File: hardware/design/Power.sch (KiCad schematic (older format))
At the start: 11 parts

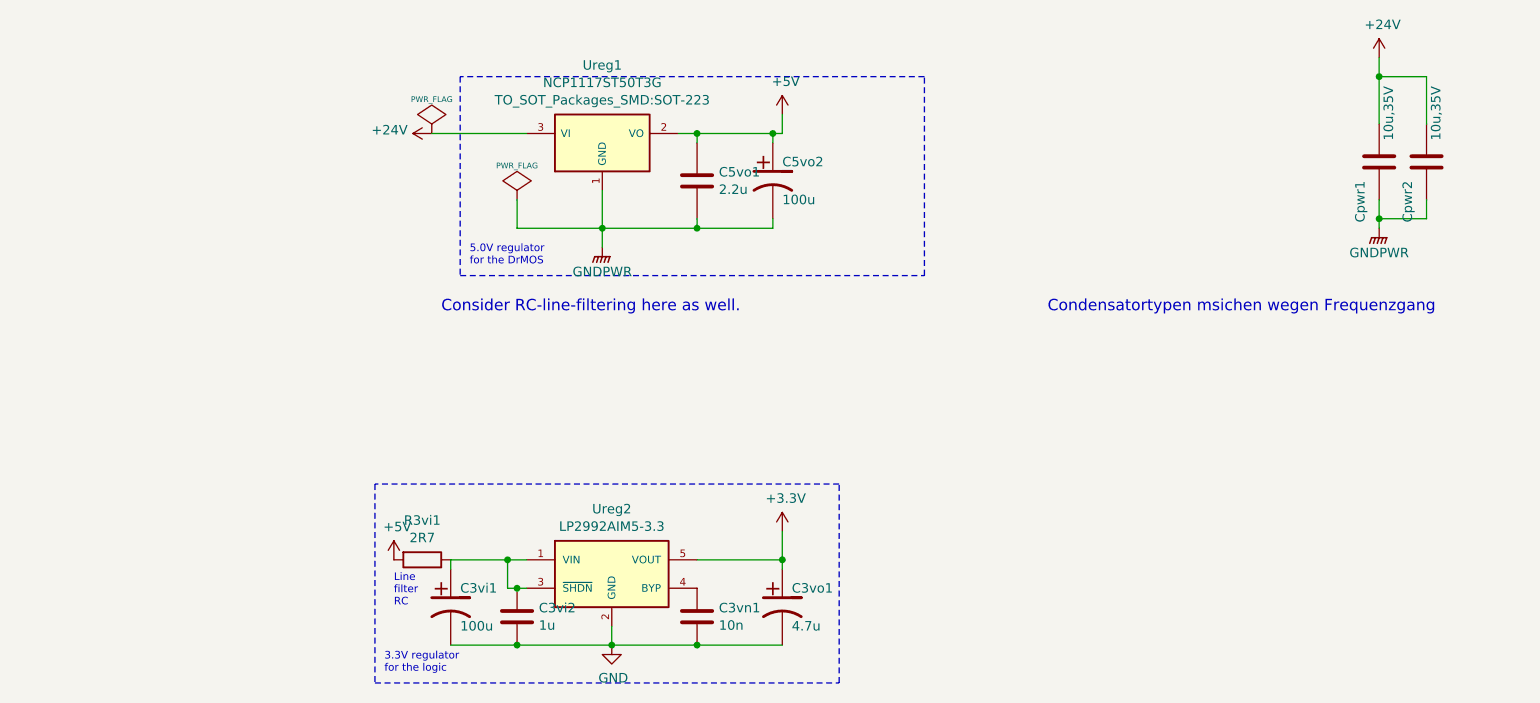
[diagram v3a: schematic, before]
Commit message: Created new component and footprint for regulator LTM8020.
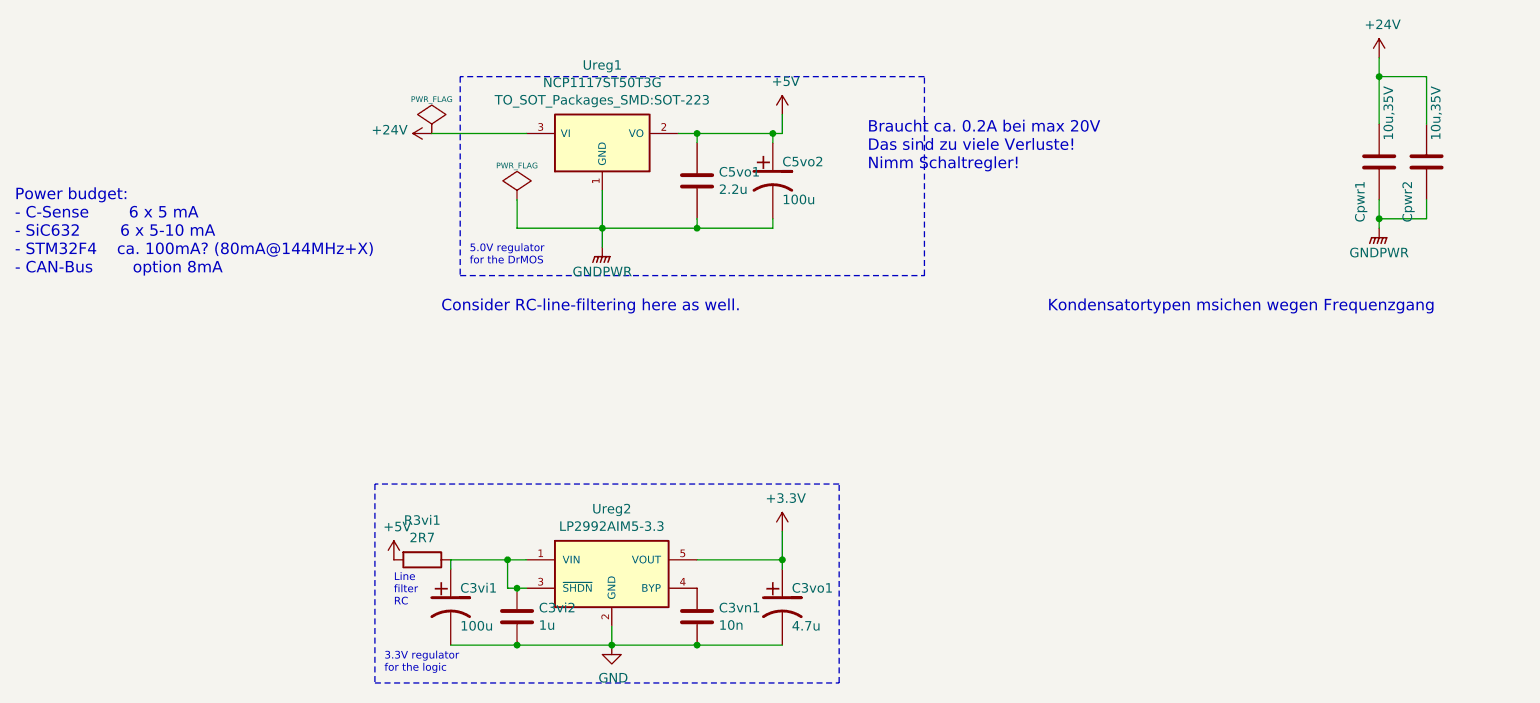
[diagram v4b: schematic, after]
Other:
- note added: "Braucht ca. 0.2A bei max 20V\nDas sind zu viele Verluste!\nNimm Schaltregler!"
- note added: "Kondensatortypen msichen wegen Frequenzgang"
- note added: "Power budget:\n- C-Sense 6 x 5 mA\n- SiC632 6 x 5-10 mA\n- STM32F4 ca. 100mA? (80mA@144MHz+X)\n- CAN-Bus option 8mA"
- note removed: "Condensatortypen msichen wegen Frequenzgang"
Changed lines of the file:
@@
 $Descr A4 11693 8268
 encoding utf-8
-Sheet 5 11
+Sheet 4 11
 Title "DrChibi"
 Date "25 Aug 2014"
@@
 00 FD 87 A8 17 00 00 00 00 F4 1F A2 5E 00 00 00 00 D0 7F 88 7A 01 00 00 00 40 FF 21 EA 05 00 00
 00 00 FD 87 A8 17 00 00 00 00 F4 1F A2 5E 00 00 00 00 D0 7F 88 7A 01 00 00 00 40 FF 21 EA 05 00
-00 00 00 FD F7 3F 90 37 91 24 49 74 FD E2 00 00 00 00 49 45 4E 44 AE 42 60 82 0F
+00 00 00 FD F7 3F 90 37 91 24 49 74 FD E2 00 00 00 00 49 45 4E 44 AE 42 60 82 00
 EndData
 $EndBitmap
@@
 AB D8 39 0B 59 91 9E DF A8 2A 5B EE 54 3A FD 71 ED 71 2F 29 C3 82 EC 80 87 06 6E C3 98 10 30 3B
 62 9A BB 2D 03 B8 C4 64 FC B5 26 AC 13 9B D1 39 40 41 C1 D6 78 4C 84 BF 94 F0 6F E1 BF 96 F0 0F
-FF 77 E2 FF 1F 0F 43 55 32 21 1C 08 16 00 00 00 00 49 45 4E 44 AE 42 60 82 EE
+FF 77 E2 FF 1F 0F 43 55 32 21 1C 08 16 00 00 00 00 49 45 4E 44 AE 42 60 82 A8
 EndData
 $EndBitmap
@@
 Connection ~ 5850 3850
 Text Notes 8650 2100 0    60   ~ 0
-Condensatortypen msichen wegen Frequenzgang
+Kondensatortypen msichen wegen Frequenzgang
 Text Notes 5200 3650 0    40   ~ 0
 Line\nfilter\nRC
 Text Notes 5450 2100 0    60   ~ 0
 Consider RC-line-filtering here as well.
+Text Notes 7700 1350 0    60   ~ 0
+Braucht ca. 0.2A bei max 20V\nDas sind zu viele Verluste!\nNimm Schaltregler!
+Text Notes 3200 1900 0    60   ~ 0
+Power budget:\n- C-Sense		6 x 5 mA\n- SiC632		6 x 5-10 mA\n- STM32F4	ca. 100mA? (80mA@144MHz+X)\n- CAN-Bus		option 8mA
 $EndSCHEMATC

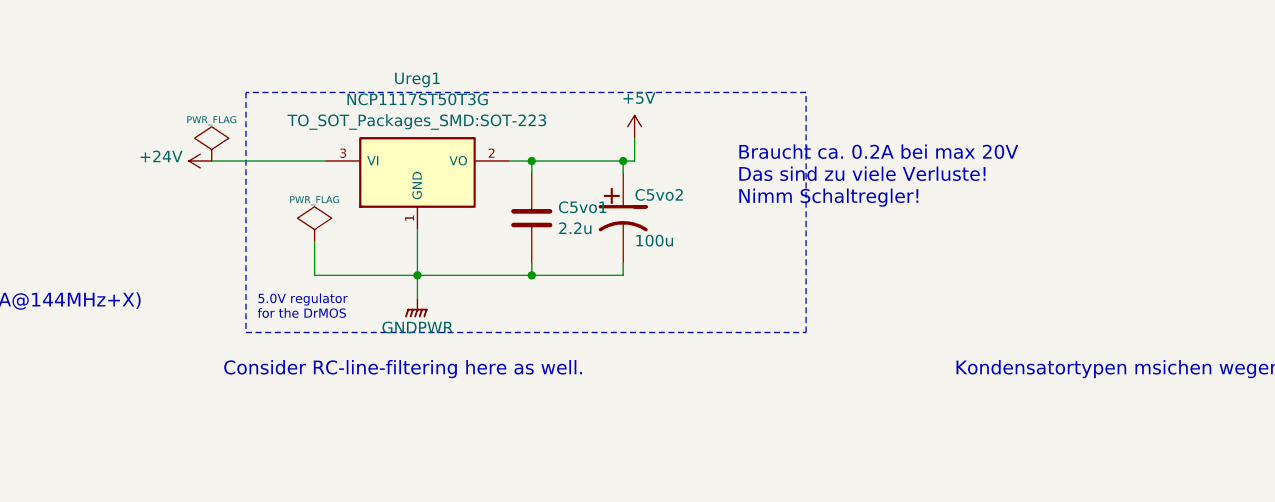
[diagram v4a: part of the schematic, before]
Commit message: Added the 5V regulator LTM8020 to the schematic.
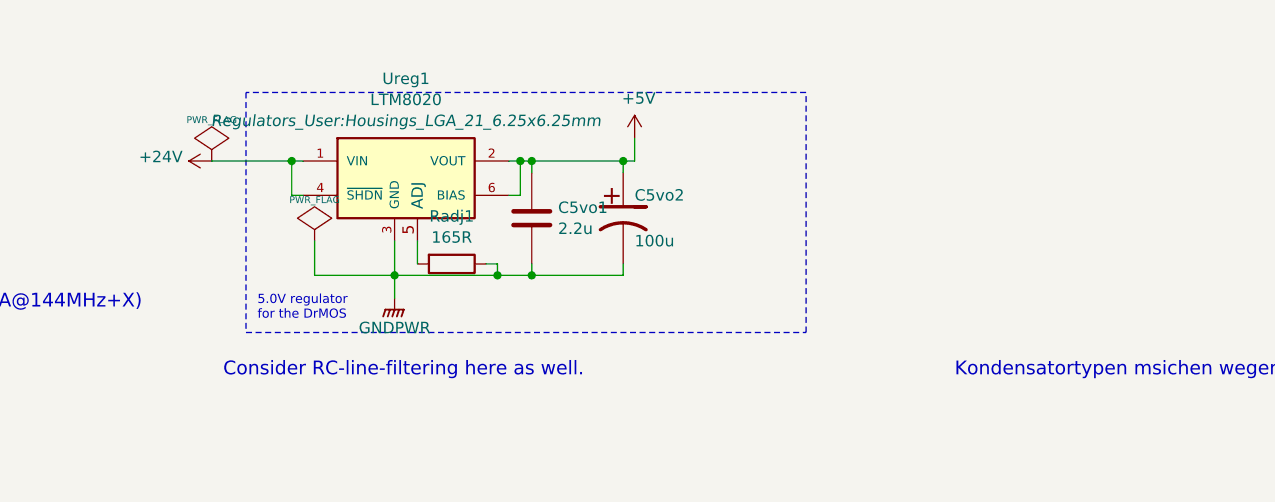
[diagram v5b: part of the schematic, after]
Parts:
- removed Ureg1: NCP1117ST50T3G, TO_SOT_Packages_SMD:SOT-223, symbol NCP1117ST50T3G
- added Radj1: 165R, Resistors_SMD:R_0402, symbol R
- added Ureg1: LTM8020, Regulators_User:Housings_LGA_21_6.25x6.25mm, symbol LTM8020
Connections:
- net +24V: now also Ureg1.1 (VIN), Ureg1.4 (~SHDN~)
- net +5V: now also Ureg1.2 (VOUT), Ureg1.6 (BIAS)
- net GNDPWR: now also Radj1.1, Ureg1.3 (GND)
- new net: Radj1.2, Ureg1.5 (ADJ)
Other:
- note removed: "Braucht ca. 0.2A bei max 20V\nDas sind zu viele Verluste!\nNimm Schaltregler!"
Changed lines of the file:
@@
 LIBS:pkl_drmos
 LIBS:pkl_misc
+LIBS:pkl_regulator
 LIBS:DrChibi-cache
 EELAYER 25 0
@@
 	7200 1650 7200 1600
 Wire Wire Line
-	6300 1450 6300 1750
-Wire Wire Line
 	6800 1650 6800 1600
-Connection ~ 6300 1650
+Connection ~ 6200 1650
 Wire Wire Line
 	7250 1150 7250 1050
@@
 AB D8 39 0B 59 91 9E DF A8 2A 5B EE 54 3A FD 71 ED 71 2F 29 C3 82 EC 80 87 06 6E C3 98 10 30 3B
 62 9A BB 2D 03 B8 C4 64 FC B5 26 AC 13 9B D1 39 40 41 C1 D6 78 4C 84 BF 94 F0 6F E1 BF 96 F0 0F
-FF 77 E2 FF 1F 0F 43 55 32 21 1C 08 16 00 00 00 00 49 45 4E 44 AE 42 60 82 A8
+FF 77 E2 FF 1F 0F 43 55 32 21 1C 08 16 00 00 00 00 49 45 4E 44 AE 42 60 82 14
 EndData
 $EndBitmap
-Wire Wire Line
-	5900 1150 5400 1150
 $Comp
 L GNDPWR #PWR030
 U 1 1 55E7501A
-P 6300 1750
-F 0 "#PWR030" H 6300 1550 50  0001 C CNN
-F 1 "GNDPWR" H 6300 1620 50  0000 C CNN
-F 2 "" H 6300 1700 60  0000 C CNN
-F 3 "" H 6300 1700 60  0000 C CNN
-	1    6300 1750
+P 6200 1750
+F 0 "#PWR030" H 6200 1550 50  0001 C CNN
+F 1 "GNDPWR" H 6200 1620 50  0000 C CNN
+F 2 "" H 6200 1700 60  0000 C CNN
+F 3 "" H 6200 1700 60  0000 C CNN
+	1    6200 1750
 	1    0    0    -1
 $EndComp
@@
 $EndComp
 $Comp
-L NCP1117ST50T3G Ureg1
-U 1 1 56A901A9
-P 6300 1200
-F 0 "Ureg1" H 6300 1610 50  0000 C CNN
-F 1 "NCP1117ST50T3G" H 6300 1518 50  0000 C CNN
-F 2 "TO_SOT_Packages_SMD:SOT-223" H 6300 1426 50  0000 C CNN
-F 3 "" H 6300 1200 50  0000 C CNN
-	1    6300 1200
-	1    0    0    -1
-$EndComp
-$Comp
 L +5V #PWR034
 U 1 1 56A9035F
@@
 Text Notes 5450 2100 0    60   ~ 0
 Consider RC-line-filtering here as well.
-Text Notes 7700 1350 0    60   ~ 0
-Braucht ca. 0.2A bei max 20V\nDas sind zu viele Verluste!\nNimm Schaltregler!
 Text Notes 3200 1900 0    60   ~ 0
 Power budget:\n- C-Sense		6 x 5 mA\n- SiC632		6 x 5-10 mA\n- STM32F4	ca. 100mA? (80mA@144MHz+X)\n- CAN-Bus		option 8mA
+$Comp
+L LTM8020 Ureg1
+U 1 1 575F2868
+P 6250 1200
+F 0 "Ureg1" H 6250 1610 50  0000 C CNN
+F 1 "LTM8020" H 6250 1518 50  0000 C CNN
+F 2 "Regulators_User:Housings_LGA_21_6.25x6.25mm" H 6250 1426 50  0000 C CIN
+F 3 "" H 6250 1200 50  0000 C CNN
+	1    6250 1200
+	1    0    0    -1
+$EndComp
+Wire Wire Line
+	6200 1500 6200 1750
+Wire Wire Line
+	5800 1150 5400 1150
+Wire Wire Line
+	6700 1300 6750 1300
+Wire Wire Line
+	6750 1300 6750 1150
+Connection ~ 6750 1150
+Wire Wire Line
+	5800 1300 5750 1300
+Wire Wire Line
+	5750 1300 5750 1150
+Connection ~ 5750 1150
+$Comp
+L R Radj1
+U 1 1 575F5779
+P 6450 1600
+F 0 "Radj1" V 6242 1600 50  0000 C CNN
+F 1 "165R" V 6334 1600 50  0000 C CNN
+F 2 "Resistors_SMD:R_0402" V 6380 1600 50  0001 C CNN
+F 3 "" H 6450 1600 50  0000 C CNN
+	1    6450 1600
+	0    1    1    0
+$EndComp
+Wire Wire Line
+	6300 1600 6300 1500
+Wire Wire Line
+	6600 1600 6650 1600
+Wire Wire Line
+	6650 1600 6650 1650
+Connection ~ 6650 1650
 $EndSCHEMATC

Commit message: Do DRC check!
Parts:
- Cpwr1: value 10u,35V -> 4.7u,35V; footprint Capacitors_SMD:C_1206 -> Capacitors_SMD:C_0805
- R3vi1: footprint Resistors_SMD:R_1206 -> Resistors_SMD:R_0805
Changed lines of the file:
@@
 P 10400 1300
 F 0 "Cpwr1" V 10500 1400 50  0000 L CNN
-F 1 "10u,35V" V 10350 900 50  0000 L CNN
-F 2 "Capacitors_SMD:C_1206" H 10400 1300 60  0001 C CNN
+F 1 "4.7u,35V" V 10350 900 50  0000 L CNN
+F 2 "Capacitors_SMD:C_0805" H 10400 1300 60  0001 C CNN
 F 3 "" H 10400 1300 60  0001 C CNN
 F 4 "X7R, e.g. GRM32ER7YA106KA12L" V 10400 1300 60  0001 C CNN "Comment"
@@
 00 FD 87 A8 17 00 00 00 00 F4 1F A2 5E 00 00 00 00 D0 7F 88 7A 01 00 00 00 40 FF 21 EA 05 00 00
 00 00 FD 87 A8 17 00 00 00 00 F4 1F A2 5E 00 00 00 00 D0 7F 88 7A 01 00 00 00 40 FF 21 EA 05 00
-00 00 00 FD F7 3F 90 37 91 24 49 74 FD E2 00 00 00 00 49 45 4E 44 AE 42 60 82 00
+00 00 00 FD F7 3F 90 37 91 24 49 74 FD E2 00 00 00 00 49 45 4E 44 AE 42 60 82 02
 EndData
 $EndBitmap
@@
 AB D8 39 0B 59 91 9E DF A8 2A 5B EE 54 3A FD 71 ED 71 2F 29 C3 82 EC 80 87 06 6E C3 98 10 30 3B
 62 9A BB 2D 03 B8 C4 64 FC B5 26 AC 13 9B D1 39 40 41 C1 D6 78 4C 84 BF 94 F0 6F E1 BF 96 F0 0F
-FF 77 E2 FF 1F 0F 43 55 32 21 1C 08 16 00 00 00 00 49 45 4E 44 AE 42 60 82 44
+FF 77 E2 FF 1F 0F 43 55 32 21 1C 08 16 00 00 00 00 49 45 4E 44 AE 42 60 82 86
 EndData
 $EndBitmap
@@
 F 0 "R3vi1" V 5142 3400 50  0000 C CNN
 F 1 "2R7" V 5234 3400 50  0000 C CNN
-F 2 "Resistors_SMD:R_1206" V 5280 3400 50  0001 C CNN
+F 2 "Resistors_SMD:R_0805" V 5280 3400 50  0001 C CNN
 F 3 "" H 5350 3400 50  0000 C CNN
 F 4 "Filter resistor to Has to dissipate 1/4W." V 5350 3400 60  0001 C CNN "Comment"
